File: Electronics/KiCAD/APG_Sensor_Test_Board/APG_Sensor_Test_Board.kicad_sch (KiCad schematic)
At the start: 13 parts, among them J1 Conn_01x02, J2 Conn_01x05, J3 Conn_01x05, J4 Conn_01x03

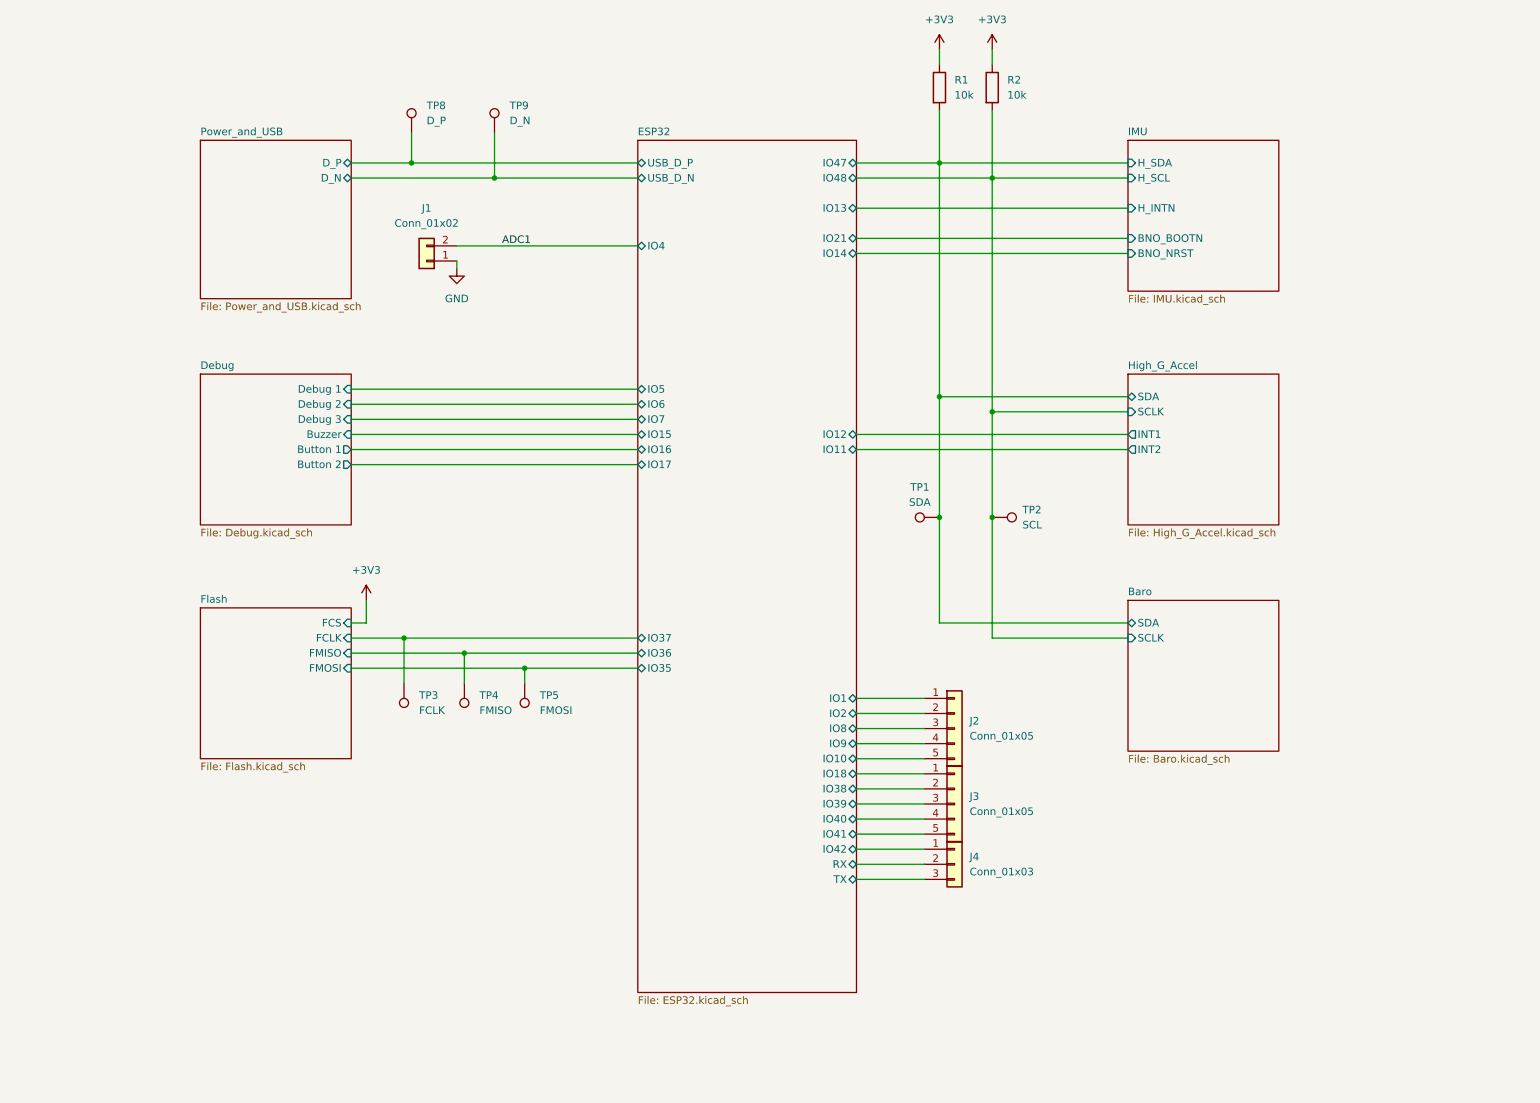
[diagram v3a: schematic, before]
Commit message: MOved IMU and HIGH G to SPI other misc changes
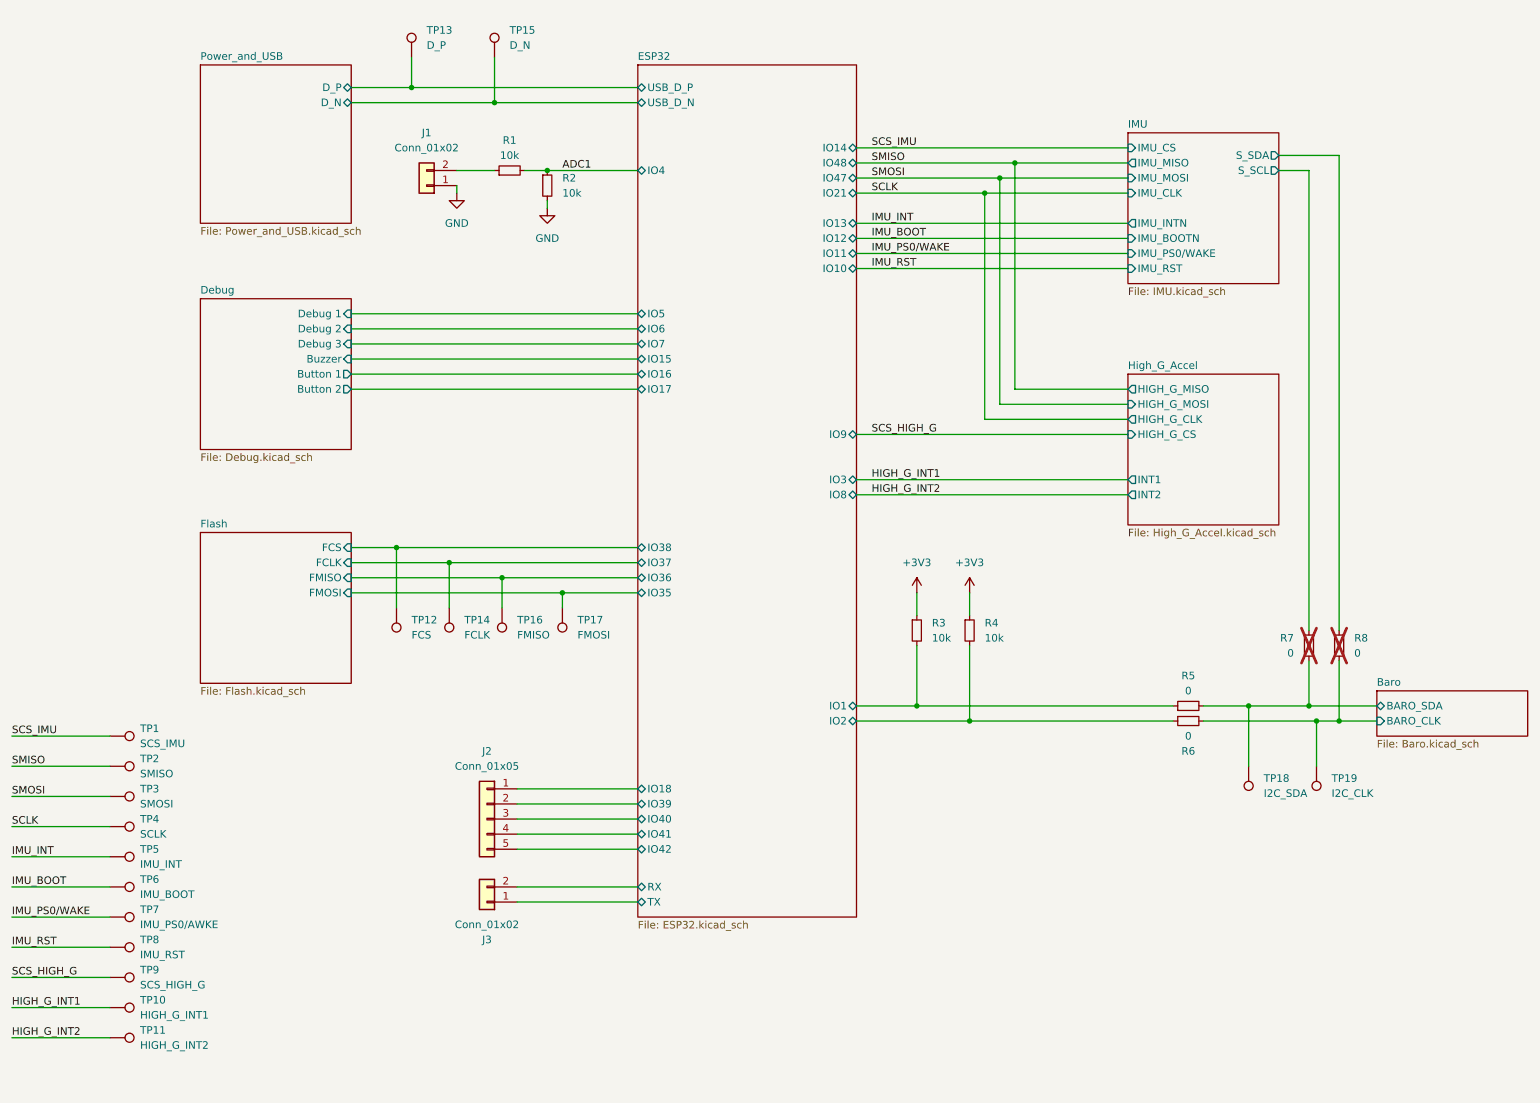
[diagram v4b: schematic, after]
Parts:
- removed J3: Conn_01x05, Connector_PinHeader_2.54mm:PinHeader_1x05_P2.54mm_Vertical, symbol Connector_Generic:Conn_01x05
- removed J4: Conn_01x03, Connector_PinHeader_2.54mm:PinHeader_1x03_P2.54mm_Vertical, symbol Connector_Generic:Conn_01x03
- removed R1, R2: 10k, Resistor_SMD:R_0805_2012Metric, symbol Device:R
- added J3: Conn_01x02, Connector_PinHeader_2.54mm:PinHeader_1x02_P2.54mm_Vertical, symbol Connector_Generic:Conn_01x02
- added R1, R2, R3, R4: 10k, Resistor_SMD:R_0805_2012Metric, symbol Device:R_Small
- added R5, R6, R7, R8: 0, Resistor_SMD:R_0805_2012Metric, symbol Device:R_Small
- added TP10: HIGH_G_INT1, TestPoint:TestPoint_Pad_3.0x3.0mm, symbol Connector:TestPoint
- added TP11: HIGH_G_INT2, TestPoint:TestPoint_Pad_3.0x3.0mm, symbol Connector:TestPoint
- added TP12: FCS, TestPoint:TestPoint_Pad_3.0x3.0mm, symbol Connector:TestPoint
- added TP18: I2C_SDA, TestPoint:TestPoint_Pad_3.0x3.0mm, symbol Connector:TestPoint
- added TP19: I2C_CLK, TestPoint:TestPoint_Pad_3.0x3.0mm, symbol Connector:TestPoint
- added TP3: SMOSI, TestPoint:TestPoint_Pad_3.0x3.0mm, symbol Connector:TestPoint
- added TP4: SCLK, TestPoint:TestPoint_Pad_3.0x3.0mm, symbol Connector:TestPoint
- added TP5: IMU_INT, TestPoint:TestPoint_Pad_3.0x3.0mm, symbol Connector:TestPoint
- added TP6: IMU_BOOT, TestPoint:TestPoint_Pad_3.0x3.0mm, symbol Connector:TestPoint
- added TP7: IMU_PS0/AWKE, TestPoint:TestPoint_Pad_3.0x3.0mm, symbol Connector:TestPoint
- added TP8: IMU_RST, TestPoint:TestPoint_Pad_3.0x3.0mm, symbol Connector:TestPoint
- added TP9: SCS_HIGH_G, TestPoint:TestPoint_Pad_3.0x3.0mm, symbol Connector:TestPoint
- TP1: value SDA -> SCS_IMU; footprint (none) -> TestPoint:TestPoint_Pad_3.0x3.0mm
- TP13: renamed from TP8; footprint (none) -> TestPoint:TestPoint_Pad_3.0x3.0mm
- TP14: renamed from TP3; footprint (none) -> TestPoint:TestPoint_Pad_3.0x3.0mm
- TP15: renamed from TP9; footprint (none) -> TestPoint:TestPoint_Pad_3.0x3.0mm
- TP16: renamed from TP4; footprint (none) -> TestPoint:TestPoint_Pad_3.0x3.0mm
- TP17: renamed from TP5; footprint (none) -> TestPoint:TestPoint_Pad_3.0x3.0mm
- TP2: value SCL -> SMISO; footprint (none) -> TestPoint:TestPoint_Pad_3.0x3.0mm
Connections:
- net ESP32/IO10 is gone; now on net ESP32/IO42: J2.5 (Pin_5)
- net ESP32/IO8 is gone; now on net ESP32/IO40: J2.3 (Pin_3)
- net ESP32/IO9 is gone; now on net ESP32/IO41: J2.4 (Pin_4)
- net +3V3: now also R3.1, R4.1
- net ADC1: now also R1.2, R2.1; no longer J1.2 (Pin_2)
- net ESP32/IO1: now also R3.2, R5.1; no longer J2.1 (Pin_1)
- net ESP32/IO18: now also J2.1 (Pin_1)
- net ESP32/IO2: now also R4.2, R6.1; no longer J2.2 (Pin_2)
- net ESP32/IO38: now also TP12.1
- net ESP32/IO39: now also J2.2 (Pin_2)
- net ESP32/RX: now also J3.2 (Pin_2)
- net ESP32/TX: now also J3.1 (Pin_1)
- net GND: now also R2.2
- net Baro/SCLK renamed SMISO
- net Baro/SDA renamed SCS_IMU
- new net: J1.2 (Pin_2), R1.1
- new net Baro/BARO_CLK: R6.2, R8.1, TP19.1
- new net Baro/BARO_SDA: R5.2, R7.1, TP18.1
- new net HIGH_G_INT1: TP10.1
- new net HIGH_G_INT2: TP11.1
- new net IMU/S_SCL: R7.2
- new net IMU/S_SDA: R8.2
- new net IMU_BOOT: TP6.1
- new net IMU_INT: TP5.1
- new net IMU_PS0/WAKE: TP7.1
- new net IMU_RST: TP8.1
- new net SCLK: TP4.1
- new net SCS_HIGH_G: TP9.1
- new net SMOSI: TP3.1
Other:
- sheet Baro ports: added BARO_CLK, BARO_SDA; removed SCLK, SDA
- sheet ESP32 ports: added IO3; removed none
- sheet High_G_Accel ports: added HIGH_G_CLK, HIGH_G_CS, HIGH_G_MISO, HIGH_G_MOSI; removed SCLK, SDA
- sheet IMU ports: added IMU_BOOTN, IMU_CLK, IMU_CS, IMU_INTN, IMU_MISO, IMU_MOSI, IMU_PS0/WAKE, IMU_RST, S_SCL, S_SDA; removed BNO_BOOTN, BNO_NRST, H_INTN, H_SCL, H_SDA
- moved on the sheet: J1, TP13, TP14, TP15, TP16, TP17

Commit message: Layout and routing
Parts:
- removed J2: Conn_01x05, Connector_PinHeader_2.54mm:PinHeader_1x05_P2.54mm_Vertical, symbol Connector_Generic:Conn_01x05
- removed TP6: IMU_BOOT, TestPoint:TestPoint_Pad_3.0x3.0mm, symbol Connector:TestPoint
- added H1, H2, H3, H4: MountingHole, MountingHole:MountingHole_3.2mm_M3, symbol Mechanical:MountingHole
- added J2: Conn_01x06, Connector_PinHeader_2.54mm:PinHeader_1x06_P2.54mm_Vertical, symbol Connector_Generic:Conn_01x06
- R1, R2, R3, R4, R5, R6, R7, R8: footprint Resistor_SMD:R_0805_2012Metric -> Resistor_SMD:R_0603_1608Metric
- TP1, TP10, TP11, TP12, TP13, TP14, TP15, TP16, TP17, TP18, TP19, TP2, TP3, TP4, TP5, TP7, TP8, TP9: footprint TestPoint:TestPoint_Pad_3.0x3.0mm -> TestPoint:TestPoint_Pad_D1.0mm
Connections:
- net Baro/BARO_CLK: now also R7.1; no longer R8.1
- net Baro/BARO_SDA: now also R8.1; no longer R7.1
- net ESP32/IO1: now also TP12.1; no longer R3.2, R5.1
- net ESP32/IO18: now also J2.2 (Pin_2)
- net ESP32/IO2: now also TP16.1; no longer R4.2, R6.1
- net ESP32/IO35: now also R4.2, R6.1; no longer TP17.1
- net ESP32/IO36: now also R3.2, R5.1; no longer TP16.1
- net ESP32/IO38: now also TP17.1; no longer TP12.1
- net ESP32/IO39: now also J2.3 (Pin_3)
- net ESP32/IO40: now also J2.4 (Pin_4)
- net ESP32/IO41: now also J2.5 (Pin_5)
- net ESP32/IO42: now also J2.6 (Pin_6)
- new net ESP32/IO8: J2.1 (Pin_1)
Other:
- sheet IMU ports: added none; removed IMU_BOOTN

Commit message: layout changes
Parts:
- removed TP13: D_P, TestPoint:TestPoint_Pad_D1.0mm, symbol Connector:TestPoint
- removed TP15: D_N, TestPoint:TestPoint_Pad_D1.0mm, symbol Connector:TestPoint
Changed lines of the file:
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@@
 	)
 	(junction
-		(at 96.52 30.48)
-		(diameter 0)
-		(color 0 0 0 0)
-	)
-	(junction
 		(at 80.01 105.41)
 		(diameter 0)
@@
 	)
 	(junction
-		(at 82.55 27.94)
-		(diameter 0)
-		(color 0 0 0 0)
-	)
-	(junction
 		(at 181.61 43.18)
 		(diameter 0)
@@
 	(wire
 		(pts
-			(xy 96.52 30.48) (xy 120.65 30.48)
-		)
-		(stroke
-			(width 0)
-			(type default)
-		)
-	)
-	(wire
-		(pts
 			(xy 88.9 107.95) (xy 88.9 115.57)
 		)
@@
 	(wire
 		(pts
-			(xy 72.39 27.94) (xy 82.55 27.94)
+			(xy 72.39 27.94) (xy 120.65 27.94)
 		)
 		(stroke
@@
 	(wire
 		(pts
-			(xy 72.39 30.48) (xy 96.52 30.48)
-		)
-		(stroke
-			(width 0)
-			(type default)
-		)
-	)
-	(wire
-		(pts
-			(xy 82.55 27.94) (xy 120.65 27.94)
+			(xy 72.39 30.48) (xy 120.65 30.48)
 		)
 		(stroke
@@
 	(wire
 		(pts
-			(xy 82.55 22.86) (xy 82.55 27.94)
-		)
-		(stroke
-			(width 0)
-			(type default)
-		)
-	)
-	(wire
-		(pts
 			(xy 203.2 83.82) (xy 179.07 83.82)
 		)
@@
 	(wire
 		(pts
-			(xy 96.52 22.86) (xy 96.52 30.48)
-		)
-		(stroke
-			(width 0)
-			(type default)
-		)
-	)
-	(wire
-		(pts
 			(xy 100.33 156.21) (xy 120.65 156.21)
 		)
@@
 	(symbol
 		(lib_id "Connector:TestPoint")
-		(at 96.52 22.86 0)
-		(unit 1)
-		(exclude_from_sim no)
-		(in_bom yes)
-		(on_board yes)
-		(dnp no)
-		(fields_autoplaced yes)
-		(property "Reference" "TP15"
-			(at 99.06 18.2879 0)
-			(effects
-				(font
-					(size 1.27 1.27)
-				)
-				(justify left)
-			)
-		)
-		(property "Value" "D_N"
-			(at 99.06 20.8279 0)
-			(effects
-				(font
-					(size 1.27 1.27)
-				)
-				(justify left)
-			)
-		)
-		(property "Footprint" "TestPoint:TestPoint_Pad_D1.0mm"
-			(at 101.6 22.86 0)
-			(effects
-				(font
-					(size 1.27 1.27)
-				)
-				(hide yes)
-			)
-		)
-		(property "Datasheet" "~"
-			(at 101.6 22.86 0)
-			(effects
-				(font
-					(size 1.27 1.27)
-				)
-				(hide yes)
-			)
-		)
-		(property "Description" "test point"
-			(at 96.52 22.86 0)
-			(effects
-				(font
-					(size 1.27 1.27)
-				)
-				(hide yes)
-			)
-		)
-		(pin "1"
-		)
-		(instances
-			(project "APG_Sensor_Test_Board"
-				(path "/3161be0c-372f-463d-be0a-bab00f344057"
-					(reference "TP15")
-					(unit 1)
-				)
-			)
-		)
-	)
-	(symbol
-		(lib_id "Connector:TestPoint")
 		(at 31.75 142.24 270)
 		(unit 1)
@@
 					(unit 1)
 				)
-			)
-		)
-	)
-	(symbol
-		(lib_id "Connector:TestPoint")
-		(at 82.55 22.86 0)
-		(unit 1)
-		(exclude_from_sim no)
-		(in_bom yes)
-		(on_board yes)
-		(dnp no)
-		(fields_autoplaced yes)
-		(property "Reference" "TP13"
-			(at 85.09 18.2879 0)
-			(effects
-				(font
-					(size 1.27 1.27)
-				)
-				(justify left)
-			)
-		)
-		(property "Value" "D_P"
-			(at 85.09 20.8279 0)
-			(effects
-				(font
-					(size 1.27 1.27)
-				)
-				(justify left)
-			)
-		)
-		(property "Footprint" "TestPoint:TestPoint_Pad_D1.0mm"
-			(at 87.63 22.86 0)
-			(effects
-				(font
-					(size 1.27 1.27)
-				)
-				(hide yes)
-			)
-		)
-		(property "Datasheet" "~"
-			(at 87.63 22.86 0)
-			(effects
-				(font
-					(size 1.27 1.27)
-				)
-				(hide yes)
-			)
-		)
-		(property "Description" "test point"
-			(at 82.55 22.86 0)
-			(effects
-				(font
-					(size 1.27 1.27)
-				)
-				(hide yes)
-			)
-		)
-		(pin "1"
-		)
-		(instances
-			(project "APG_Sensor_Test_Board"
-				(path "/3161be0c-372f-463d-be0a-bab00f344057"
-					(reference "TP13")
-					(unit 1)
-				)
